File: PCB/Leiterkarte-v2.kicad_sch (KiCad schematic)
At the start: 42 parts

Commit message: Replaced oil and fuel 'pre resistor' to 240 ohms; Replaced water temp 'pre resistor' to 3k ohms; Implemented basic functionality of SensorManager (WIP); Implemented simple log-level feature
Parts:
- Rfuel1, Roil1: value 100 -> 240
- Rwtr1: value 100 -> 3k
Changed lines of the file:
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@@
 			)
 		)
-		(property "Value" "100"
+		(property "Value" "240"
 			(at 135.382 35.052 90)
 			(effects
@@
 			)
 		)
-		(property "Value" "100"
+		(property "Value" "240"
 			(at 135.382 22.86 90)
 			(effects
@@
 		(dnp no)
 		(property "Reference" "Rwtr1"
-			(at 135.382 49.022 90)
+			(at 135.382 44.958 90)
 			(effects
 				(font
@@
 			)
 		)
-		(property "Value" "100"
+		(property "Value" "3k"
 			(at 135.382 46.99 90)
 			(effects

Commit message: Implemented measurement of speed and rpm; The speed hz is measured but is not yet converted to actual kmh/mph
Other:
- note added: "The ESP32 allows 3.6V max. We only measure <500Hz, so this divider has no negative affects"
- note removed: "The STM32 allows 3.6V max. We only measure <500Hz, so this divider has no negative affects"
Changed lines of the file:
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@@
 		)
 	)
-	(text_box "- Longer pads on the USB-C port and PCB\n- Bigger JST connectors\n- More GND vias\n- Bigger Cin1 (i guess)"
-		(exclude_from_sim no)
-		(at 197.104 138.938 0)
-		(size 40.894 27.178)
+	(text_box "- Longer pads on the USB-C port and ESP\n- Bigger JST connectors\n- More GND vias\n- Bigger Cin1 (i guess)\n- Put Power Supply on the upper side\n- Pulldown for speed line\n- Maybe make one shield plane to 3.3V\n- Check MAX9926 max input voltage for the sensor"
+		(exclude_from_sim no)
+		(at 177.038 138.938 0)
+		(size 61.214 27.178)
 		(stroke
 			(width 0)
@@
 		)
 	)
-	(text "The STM32 allows 3.6V max.\nWe only measure <500Hz, so\nthis divider has no negative affects"
+	(text "The ESP32 allows 3.6V max.\nWe only measure <500Hz, so\nthis divider has no negative affects"
 		(exclude_from_sim no)
 		(at 213.106 62.23 0)

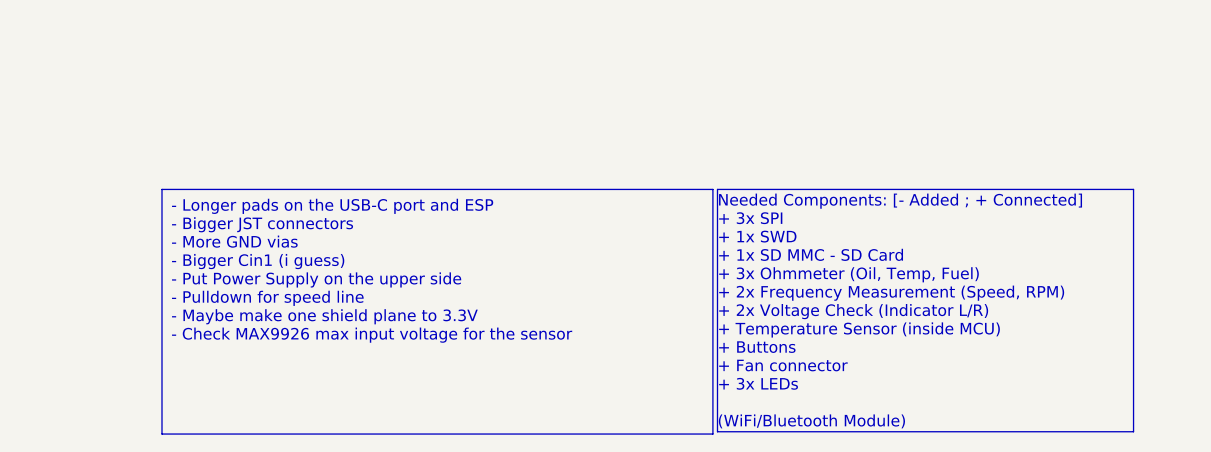
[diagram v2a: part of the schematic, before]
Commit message: Implemented reading of internal (on-board) temperature sensor
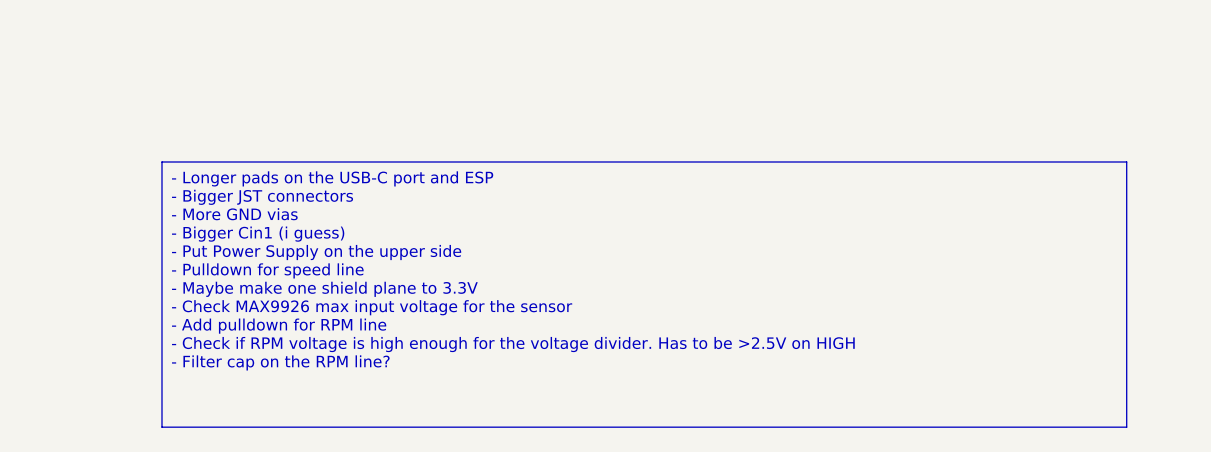
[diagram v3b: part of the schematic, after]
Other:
- note removed: "Needed Components: [- Added ; + Connected] + 3x SPI + 1x SWD + 1x SD MMC - SD Card + 3x Ohmmeter (Oil, Temp, Fuel) + 2x Frequency Measurement (Speed, RPM) + 2x Voltage Check (Indicator L/R) + Temperature Sensor (inside MCU) + Buttons + Fan connector + 3x LEDs (WiFi/Bluetooth Module)"
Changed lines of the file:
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@@
-	)
-	(rectangle
-		(start 238.76 138.938)
-		(end 284.988 165.862)
-		(stroke
-			(width 0)
-			(type default)
-		)
-		(fill
-			(type none)
-		)
 	)
 	(rectangle
@@
 		)
 	)
-	(text_box "- Longer pads on the USB-C port and ESP\n- Bigger JST connectors\n- More GND vias\n- Bigger Cin1 (i guess)\n- Put Power Supply on the upper side\n- Pulldown for speed line\n- Maybe make one shield plane to 3.3V\n- Check MAX9926 max input voltage for the sensor"
+	(text_box "- Longer pads on the USB-C port and ESP\n- Bigger JST connectors\n- More GND vias\n- Bigger Cin1 (i guess)\n- Put Power Supply on the upper side\n- Pulldown for speed line\n- Maybe make one shield plane to 3.3V\n- Check MAX9926 max input voltage for the sensor\n- Add pulldown for RPM line\n- Check if RPM voltage is high enough for the voltage divider. Has to be >2.5V on HIGH\n- Filter cap on the RPM line?"
 		(exclude_from_sim no)
-		(at 177.038 138.938 0)
-		(size 61.214 27.178)
+		(at 177.038 135.89 0)
+		(size 107.188 29.464)
 		(stroke
 			(width 0)
@@
 		(effects
 			(font
-				(size 1.27 1.27)
-			)
-			(justify left)
-		)
-	)
-	(text "Needed Components: [- Added ; + Connected]\n+ 3x SPI\n+ 1x SWD\n+ 1x SD MMC - SD Card\n+ 3x Ohmmeter (Oil, Temp, Fuel)\n+ 2x Frequency Measurement (Speed, RPM)\n+ 2x Voltage Check (Indicator L/R)\n+ Temperature Sensor (inside MCU)\n+ Buttons\n+ Fan connector\n+ 3x LEDs\n\n(WiFi/Bluetooth Module)"
-		(exclude_from_sim no)
-		(at 238.76 152.654 0)
-		(effects
-			(font
